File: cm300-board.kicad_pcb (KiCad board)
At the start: 2 copper layers, 40 x 25 mm, 13 parts, among them J1 Screw_Terminal_01x02, J2 Screw_Terminal_01x02, J3 Conn_01x04_Female

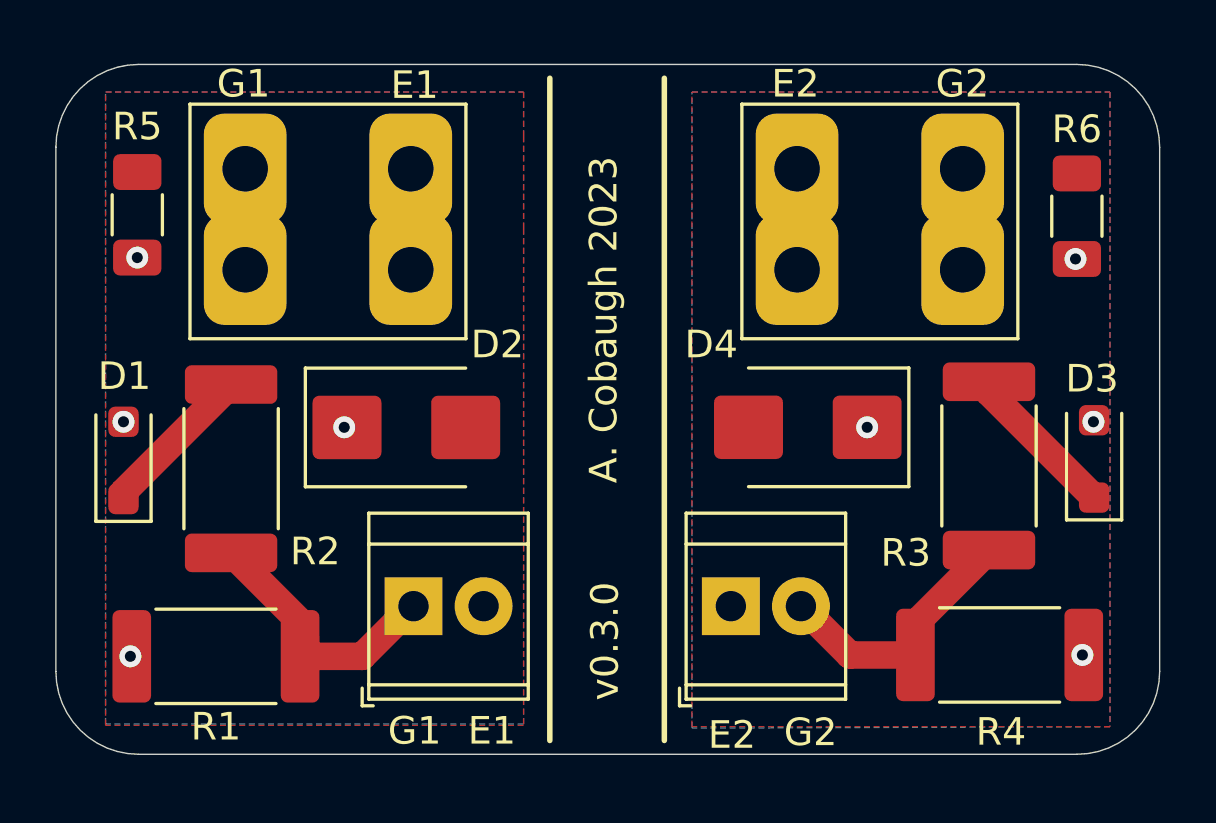
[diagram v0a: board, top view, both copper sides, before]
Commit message: feat: convert to SMD, add Rge
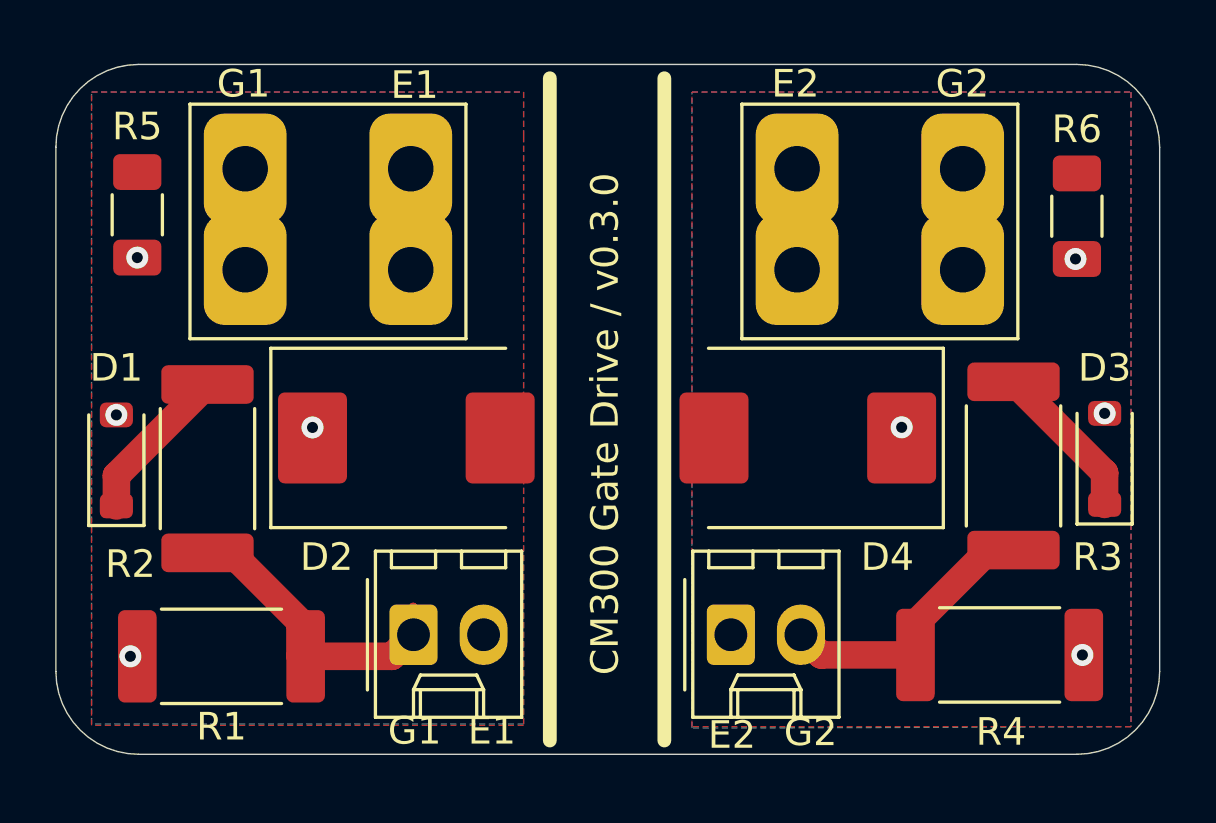
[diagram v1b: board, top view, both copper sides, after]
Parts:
- D1, D3: footprint Diode_SMD:D_SOD-123F -> Diode_SMD:D_SOD-123
- D2, D4: footprint Diode_SMD:D_SMB -> Diode_SMD:D_SMC
- J1, J2: footprint TerminalBlock_TE-Connectivity:TerminalBlock_TE_282834-2_1x02_P2.54mm_Horizontal -> Connector_Molex:Molex_KK-254_AE-6410-02A_1x02_P2.54mm_Vertical
- moved J1 1.04 mm to (-993.0, -1038.3)
- moved J2 1.04 mm to (-981.5, -1038.3)
- moved R3 0.89 mm to (-971.3, -1044.5)
- moved R2 0.86 mm to (-1000.5, -1044.3)
- moved D4 0.39 mm to (-978.8, -1045.5)
- moved D2 0.38 mm to (-993.3, -1045.5)
- moved D3 0.38 mm to (-968.0, -1044.7)
- moved D1 0.26 mm to (-1003.8, -1044.7)
- moved R1 0.20 mm to (-1000.0, -1037.5)
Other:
- board text added: "CM300 Gate Drive / v0.3.0"
- board text removed: "A. Cobaugh 2023"
- board text removed: "v0.3.0"
